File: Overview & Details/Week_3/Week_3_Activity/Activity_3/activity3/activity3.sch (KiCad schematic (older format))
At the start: 2 parts, among them J1 62684-502100ALF, U3 DISP_TFT_2.8IN_240x320_50PIN

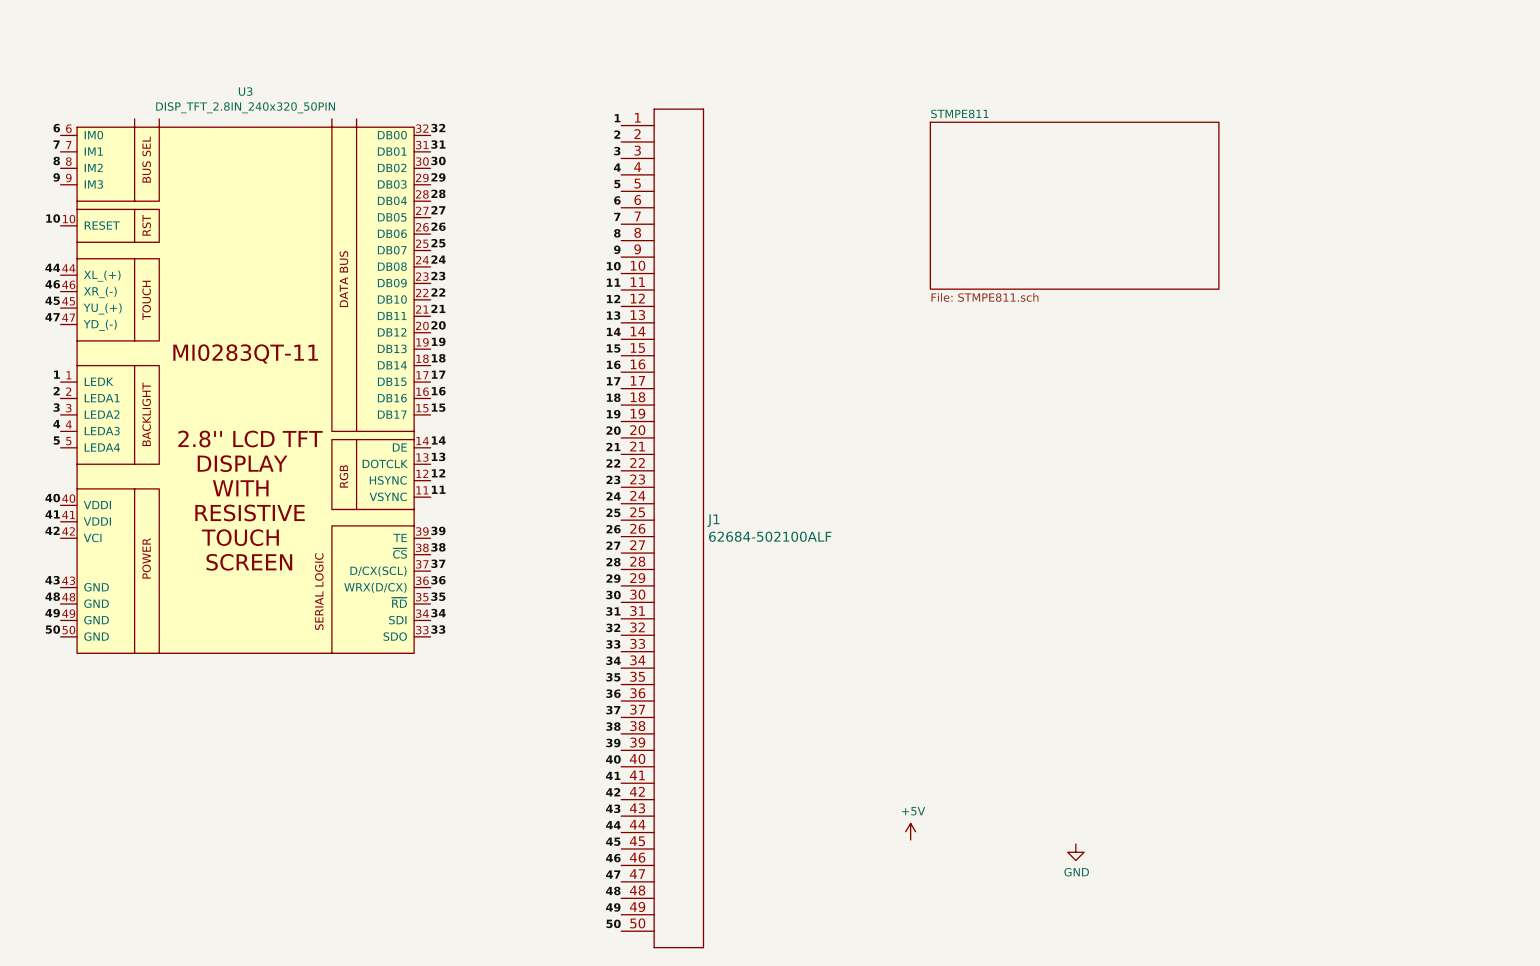
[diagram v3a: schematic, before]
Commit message: added STEMP811 controller and added pins
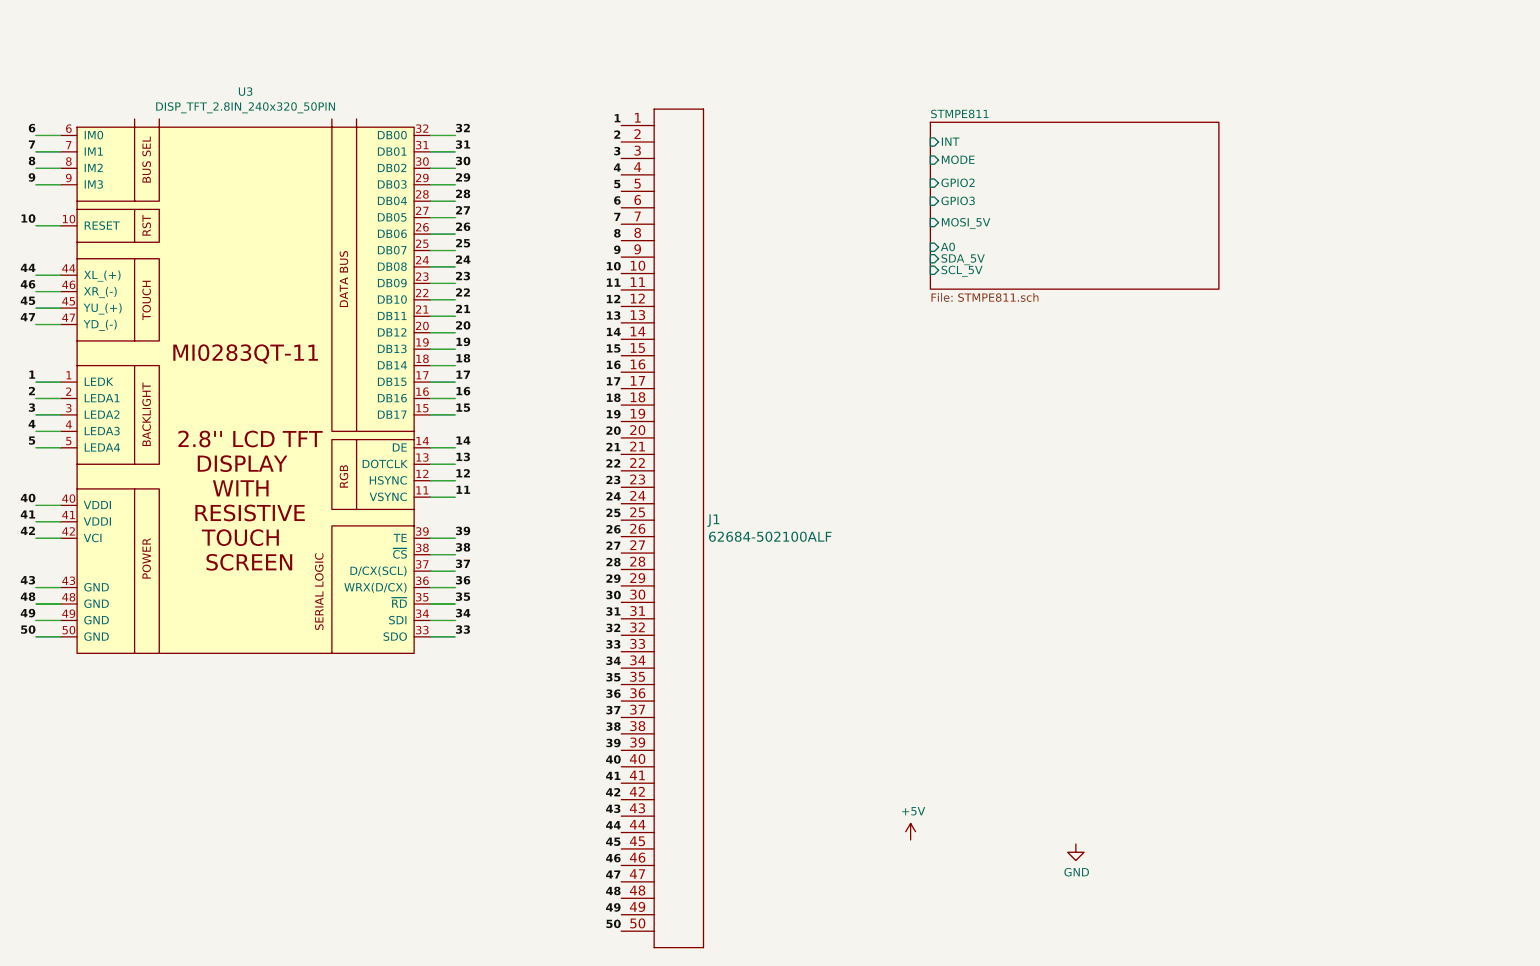
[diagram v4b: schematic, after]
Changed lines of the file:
@@
 F0 "STMPE811" 50
 F1 "STMPE811.sch" 50
+F2 "INT" I L 7330 1490 50
+F3 "MODE" I L 7330 1600 50
+F4 "GPIO2" I L 7330 1740 50
+F5 "GPIO3" I L 7330 1850 50
+F6 "MOSI_5V" I L 7330 1980 50
+F7 "A0" I L 7330 2130 50
+F8 "SCL_5V" I L 7330 2270 50
+F9 "SDA_5V" I L 7330 2200 50
 $EndSheet
 $Comp
@@
 	1    0    0    -1
 $EndComp
-Text Label 4290 1450 0    50   ~ 10
+Text Label 4440 1450 0    50   ~ 10
 32
-Text Label 4290 1550 0    50   ~ 10
+Text Label 4440 1550 0    50   ~ 10
 31
-Text Label 4290 1650 0    50   ~ 10
+Text Label 4440 1650 0    50   ~ 10
 30
-Text Label 4290 1750 0    50   ~ 10
+Text Label 4440 1750 0    50   ~ 10
 29
 Text Label 5450 4490 2    50   ~ 10
@@
 Text Label 5450 4190 2    50   ~ 10
 29
-Text Label 4290 1850 0    50   ~ 10
+Text Label 4440 1850 0    50   ~ 10
 28
-Text Label 4290 1950 0    50   ~ 10
+Text Label 4440 1950 0    50   ~ 10
 27
-Text Label 4290 2050 0    50   ~ 10
+Text Label 4440 2050 0    50   ~ 10
 26
-Text Label 4290 2150 0    50   ~ 10
+Text Label 4440 2150 0    50   ~ 10
 25
-Text Label 4290 2250 0    50   ~ 10
+Text Label 4440 2250 0    50   ~ 10
 24
-Text Label 4290 2350 0    50   ~ 10
+Text Label 4440 2350 0    50   ~ 10
 23
-Text Label 4290 2450 0    50   ~ 10
+Text Label 4440 2450 0    50   ~ 10
 22
-Text Label 4290 2550 0    50   ~ 10
+Text Label 4440 2550 0    50   ~ 10
 21
-Text Label 4290 2650 0    50   ~ 10
+Text Label 4440 2650 0    50   ~ 10
 20
-Text Label 4290 2750 0    50   ~ 10
+Text Label 4440 2750 0    50   ~ 10
 19
-Text Label 4290 2850 0    50   ~ 10
+Text Label 4440 2850 0    50   ~ 10
 18
-Text Label 4290 2950 0    50   ~ 10
+Text Label 4440 2950 0    50   ~ 10
 17
-Text Label 4290 3050 0    50   ~ 10
+Text Label 4440 3050 0    50   ~ 10
 16
-Text Label 4290 3150 0    50   ~ 10
+Text Label 4440 3150 0    50   ~ 10
 15
 Text Label 5450 4090 2    50   ~ 10
@@
 Text Label 5450 2790 2    50   ~ 10
 15
-Text Label 4290 3350 0    50   ~ 10
+Text Label 4440 3350 0    50   ~ 10
 14
-Text Label 4290 3450 0    50   ~ 10
+Text Label 4440 3450 0    50   ~ 10
 13
-Text Label 4290 3550 0    50   ~ 10
+Text Label 4440 3550 0    50   ~ 10
 12
-Text Label 4290 3650 0    50   ~ 10
+Text Label 4440 3650 0    50   ~ 10
 11
 Text Label 5450 2690 2    50   ~ 10
@@
 Text Label 5450 2390 2    50   ~ 10
 11
-Text Label 4290 3900 0    50   ~ 10
+Text Label 4440 3900 0    50   ~ 10
 39
-Text Label 4290 4000 0    50   ~ 10
+Text Label 4440 4000 0    50   ~ 10
 38
-Text Label 4290 4100 0    50   ~ 10
+Text Label 4440 4100 0    50   ~ 10
 37
-Text Label 4290 4200 0    50   ~ 10
+Text Label 4440 4200 0    50   ~ 10
 36
-Text Label 4290 4300 0    50   ~ 10
+Text Label 4440 4300 0    50   ~ 10
 35
-Text Label 4290 4400 0    50   ~ 10
+Text Label 4440 4400 0    50   ~ 10
 34
-Text Label 4290 4500 0    50   ~ 10
+Text Label 4440 4500 0    50   ~ 10
 33
 Text Label 5450 5190 2    50   ~ 10
@@
 Text Label 5450 4590 2    50   ~ 10
 33
-Text Label 2040 4200 2    50   ~ 10
+Text Label 1890 4200 2    50   ~ 10
 43
-Text Label 2040 3900 2    50   ~ 10
+Text Label 1890 3900 2    50   ~ 10
 42
-Text Label 2040 3800 2    50   ~ 10
+Text Label 1890 3800 2    50   ~ 10
 41
-Text Label 2040 3700 2    50   ~ 10
+Text Label 1890 3700 2    50   ~ 10
 40
 Text Label 5450 5490 2    50   ~ 10
@@
 Text Label 5450 5590 2    50   ~ 10
 43
-Text Label 2040 4300 2    50   ~ 10
+Text Label 1890 4300 2    50   ~ 10
 48
-Text Label 2040 4400 2    50   ~ 10
+Text Label 1890 4400 2    50   ~ 10
 49
-Text Label 2040 4500 2    50   ~ 10
+Text Label 1890 4500 2    50   ~ 10
 50
 $Comp
@@
 Text Label 5450 6290 2    50   ~ 10
 50
-Text Label 2040 2950 2    50   ~ 10
+Text Label 1890 2950 2    50   ~ 10
 1
-Text Label 2040 3050 2    50   ~ 10
+Text Label 1890 3050 2    50   ~ 10
 2
-Text Label 2040 3150 2    50   ~ 10
+Text Label 1890 3150 2    50   ~ 10
 3
-Text Label 2040 3250 2    50   ~ 10
+Text Label 1890 3250 2    50   ~ 10
 4
-Text Label 2040 3350 2    50   ~ 10
+Text Label 1890 3350 2    50   ~ 10
 5
 Text Label 5450 1390 2    50   ~ 10
@@
 Text Label 5450 1790 2    50   ~ 10
 5
-Text Label 2040 2600 2    50   ~ 10
+Text Label 1890 2600 2    50   ~ 10
 47
-Text Label 2040 2500 2    50   ~ 10
+Text Label 1890 2500 2    50   ~ 10
 45
-Text Label 2040 2400 2    50   ~ 10
+Text Label 1890 2400 2    50   ~ 10
 46
-Text Label 2040 2300 2    50   ~ 10
+Text Label 1890 2300 2    50   ~ 10
 44
 Text Label 5450 5990 2    50   ~ 10
@@
 Text Label 5450 5690 2    50   ~ 10
 44
-Text Label 2040 2000 2    50   ~ 10
+Text Label 1890 2000 2    50   ~ 10
 10
-Text Label 2040 1750 2    50   ~ 10
+Text Label 1890 1750 2    50   ~ 10
 9
-Text Label 2040 1650 2    50   ~ 10
+Text Label 1890 1650 2    50   ~ 10
 8
-Text Label 2040 1550 2    50   ~ 10
+Text Label 1890 1550 2    50   ~ 10
 7
-Text Label 2040 1450 2    50   ~ 10
+Text Label 1890 1450 2    50   ~ 10
 6
 Text Label 5450 2290 2    50   ~ 10
@@
 Text Label 5450 1890 2    50   ~ 10
 6
+Wire Wire Line
+	4290 4500 4440 4500
+Wire Wire Line
+	4290 4400 4440 4400
+Wire Wire Line
+	4290 4300 4440 4300
+Wire Wire Line
+	4290 4200 4440 4200
+Wire Wire Line
+	4290 4100 4440 4100
+Wire Wire Line
+	4290 4000 4440 4000
+Wire Wire Line
+	4290 3900 4440 3900
+Wire Wire Line
+	4290 3650 4440 3650
+Wire Wire Line
+	4290 3550 4440 3550
+Wire Wire Line
+	4290 3450 4440 3450
+Wire Wire Line
+	4290 3350 4440 3350
+Wire Wire Line
+	4290 3150 4440 3150
+Wire Wire Line
+	4290 3050 4440 3050
+Wire Wire Line
+	4290 2950 4440 2950
+Wire Wire Line
+	4290 2850 4440 2850
+Wire Wire Line
+	4290 2750 4440 2750
+Wire Wire Line
+	4290 2650 4440 2650
+Wire Wire Line
+	4290 2550 4440 2550
+Wire Wire Line
+	4290 2450 4440 2450
+Wire Wire Line
+	4290 2350 4440 2350
+Wire Wire Line
+	4290 2250 4440 2250
+Wire Wire Line
+	4290 2150 4440 2150
+Wire Wire Line
+	4290 2050 4440 2050
+Wire Wire Line
+	4290 1950 4440 1950
+Wire Wire Line
+	4290 1850 4440 1850
+Wire Wire Line
+	4290 1750 4440 1750
+Wire Wire Line
+	4290 1650 4440 1650
+Wire Wire Line
+	4290 1550 4440 1550
+Wire Wire Line
+	4290 1450 4440 1450
+Wire Wire Line
+	1890 1650 2040 1650
+Wire Wire Line
+	1890 1550 2040 1550
+Wire Wire Line
+	1890 1450 2040 1450
+Wire Wire Line
+	1890 2950 2040 2950
+Wire Wire Line
+	1890 2600 2040 2600
+Wire Wire Line
+	1890 2500 2040 2500
+Wire Wire Line
+	1890 2400 2040 2400
+Wire Wire Line
+	1890 2300 2040 2300
+Wire Wire Line
+	1890 2000 2040 2000
+Wire Wire Line
+	1890 1750 2040 1750
+Wire Wire Line
+	1890 3900 2040 3900
+Wire Wire Line
+	1890 3800 2040 3800
+Wire Wire Line
+	1890 3700 2040 3700
+Wire Wire Line
+	1890 3350 2040 3350
+Wire Wire Line
+	1890 3250 2040 3250
+Wire Wire Line
+	1890 3150 2040 3150
+Wire Wire Line
+	1890 3050 2040 3050
+Wire Wire Line
+	1890 4500 2040 4500
+Wire Wire Line
+	1890 4400 2040 4400
+Wire Wire Line
+	1890 4300 2040 4300
+Wire Wire Line
+	1890 4200 2040 4200
 $EndSCHEMATC

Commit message: added hierarchical pins to STMPE811
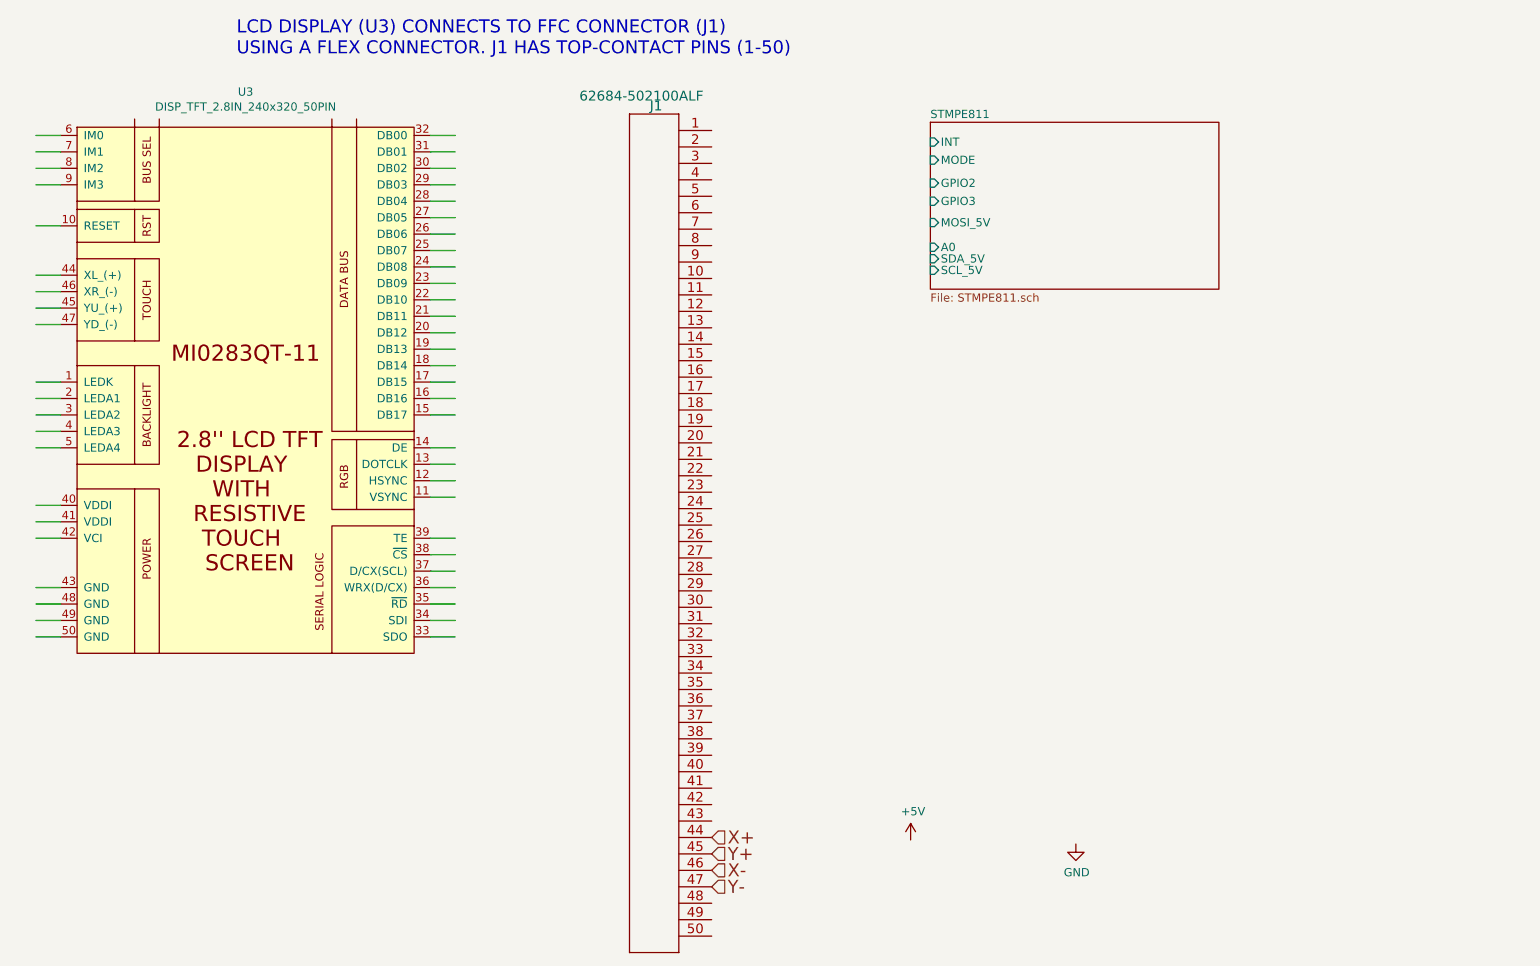
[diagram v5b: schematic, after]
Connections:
- net labels added: X+, X-, Y+, Y-
- net labels removed: 1, 10, 11, 12, 13, 14, 15, 16, 17, 18, 19, 2, 20, 21, 22, 23, 24, 25, 26, 27, 28, 29, 3, 30, 31, 32, 33, 34, 35, 36, 37, 38, 39, 4, 40, 41, 42, 43, 44, 45, 46, 47, 48, 49, 5, 50, 6, 7, 8, 9
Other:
- note added: "LCD DISPLAY (U3) CONNECTS TO FFC CONNECTOR (J1) \nUSING A FLEX CONNECTOR. J1 HAS TOP-CONTACT PINS (1-50)"
- moved on the sheet: J1
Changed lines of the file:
@@
 L 2020-04-05_01-22-35:62684-502100ALF J1
 U 1 1 5F061D23
-P 5450 1390
-F 0 "J1" H 5978 -1007 60  0000 L CNN
-F 1 "62684-502100ALF" H 5978 -1113 60  0000 L CNN
-F 2 "CONN50_62684-502100ALF" H 5850 -1070 60  0001 C CNN
-F 3 "" H 5450 1390 60  0000 C CNN
-	1    5450 1390
-	1    0    0    -1
+P 6000 1420
+F 0 "J1" H 6300 1570 60  0000 L CNN
+F 1 "62684-502100ALF" H 6050 1630 60  0000 L CNN
+F 2 "CONN50_62684-502100ALF" H 6400 -1040 60  0001 C CNN
+F 3 "" H 6000 1420 60  0000 C CNN
+	1    6000 1420
+	-1   0    0    -1
 $EndComp
-Text Label 4440 1450 0    50   ~ 10
-32
-Text Label 4440 1550 0    50   ~ 10
-31
-Text Label 4440 1650 0    50   ~ 10
-30
-Text Label 4440 1750 0    50   ~ 10
-29
-Text Label 5450 4490 2    50   ~ 10
-32
-Text Label 5450 4390 2    50   ~ 10
-31
-Text Label 5450 4290 2    50   ~ 10
-30
-Text Label 5450 4190 2    50   ~ 10
-29
-Text Label 4440 1850 0    50   ~ 10
-28
-Text Label 4440 1950 0    50   ~ 10
-27
-Text Label 4440 2050 0    50   ~ 10
-26
-Text Label 4440 2150 0    50   ~ 10
-25
-Text Label 4440 2250 0    50   ~ 10
-24
-Text Label 4440 2350 0    50   ~ 10
-23
-Text Label 4440 2450 0    50   ~ 10
-22
-Text Label 4440 2550 0    50   ~ 10
-21
-Text Label 4440 2650 0    50   ~ 10
-20
-Text Label 4440 2750 0    50   ~ 10
-19
-Text Label 4440 2850 0    50   ~ 10
-18
-Text Label 4440 2950 0    50   ~ 10
-17
-Text Label 4440 3050 0    50   ~ 10
-16
-Text Label 4440 3150 0    50   ~ 10
-15
-Text Label 5450 4090 2    50   ~ 10
-28
-Text Label 5450 3990 2    50   ~ 10
-27
-Text Label 5450 3890 2    50   ~ 10
-26
-Text Label 5450 3790 2    50   ~ 10
-25
-Text Label 5450 3690 2    50   ~ 10
-24
-Text Label 5450 3590 2    50   ~ 10
-23
-Text Label 5450 3490 2    50   ~ 10
-22
-Text Label 5450 3390 2    50   ~ 10
-21
-Text Label 5450 3290 2    50   ~ 10
-20
-Text Label 5450 3190 2    50   ~ 10
-19
-Text Label 5450 3090 2    50   ~ 10
-18
-Text Label 5450 2990 2    50   ~ 10
-17
-Text Label 5450 2890 2    50   ~ 10
-16
-Text Label 5450 2790 2    50   ~ 10
-15
-Text Label 4440 3350 0    50   ~ 10
-14
-Text Label 4440 3450 0    50   ~ 10
-13
-Text Label 4440 3550 0    50   ~ 10
-12
-Text Label 4440 3650 0    50   ~ 10
-11
-Text Label 5450 2690 2    50   ~ 10
-14
-Text Label 5450 2590 2    50   ~ 10
-13
-Text Label 5450 2490 2    50   ~ 10
-12
-Text Label 5450 2390 2    50   ~ 10
-11
-Text Label 4440 3900 0    50   ~ 10
-39
-Text Label 4440 4000 0    50   ~ 10
-38
-Text Label 4440 4100 0    50   ~ 10
-37
-Text Label 4440 4200 0    50   ~ 10
-36
-Text Label 4440 4300 0    50   ~ 10
-35
-Text Label 4440 4400 0    50   ~ 10
-34
-Text Label 4440 4500 0    50   ~ 10
-33
-Text Label 5450 5190 2    50   ~ 10
-39
-Text Label 5450 5090 2    50   ~ 10
-38
-Text Label 5450 4990 2    50   ~ 10
-37
-Text Label 5450 4890 2    50   ~ 10
-36
-Text Label 5450 4790 2    50   ~ 10
-35
-Text Label 5450 4690 2    50   ~ 10
-34
-Text Label 5450 4590 2    50   ~ 10
-33
-Text Label 1890 4200 2    50   ~ 10
-43
-Text Label 1890 3900 2    50   ~ 10
-42
-Text Label 1890 3800 2    50   ~ 10
-41
-Text Label 1890 3700 2    50   ~ 10
-40
-Text Label 5450 5490 2    50   ~ 10
-42
-Text Label 5450 5390 2    50   ~ 10
-41
-Text Label 5450 5290 2    50   ~ 10
-40
-Text Label 5450 5590 2    50   ~ 10
-43
-Text Label 1890 4300 2    50   ~ 10
-48
-Text Label 1890 4400 2    50   ~ 10
-49
-Text Label 1890 4500 2    50   ~ 10
-50
 $Comp
 L Display_Board_Lib:DISP_TFT_2.8IN_240x320_50PIN U3
@@
 	1    0    0    -1
 $EndComp
-Text Label 5450 6090 2    50   ~ 10
-48
-Text Label 5450 6190 2    50   ~ 10
-49
-Text Label 5450 6290 2    50   ~ 10
-50
-Text Label 1890 2950 2    50   ~ 10
-1
-Text Label 1890 3050 2    50   ~ 10
-2
-Text Label 1890 3150 2    50   ~ 10
-3
-Text Label 1890 3250 2    50   ~ 10
-4
-Text Label 1890 3350 2    50   ~ 10
-5
-Text Label 5450 1390 2    50   ~ 10
-1
-Text Label 5450 1490 2    50   ~ 10
-2
-Text Label 5450 1590 2    50   ~ 10
-3
-Text Label 5450 1690 2    50   ~ 10
-4
-Text Label 5450 1790 2    50   ~ 10
-5
-Text Label 1890 2600 2    50   ~ 10
-47
-Text Label 1890 2500 2    50   ~ 10
-45
-Text Label 1890 2400 2    50   ~ 10
-46
-Text Label 1890 2300 2    50   ~ 10
-44
-Text Label 5450 5990 2    50   ~ 10
-47
-Text Label 5450 5790 2    50   ~ 10
-45
-Text Label 5450 5890 2    50   ~ 10
-46
-Text Label 5450 5690 2    50   ~ 10
-44
-Text Label 1890 2000 2    50   ~ 10
-10
-Text Label 1890 1750 2    50   ~ 10
-9
-Text Label 1890 1650 2    50   ~ 10
-8
-Text Label 1890 1550 2    50   ~ 10
-7
-Text Label 1890 1450 2    50   ~ 10
-6
-Text Label 5450 2290 2    50   ~ 10
-10
-Text Label 5450 2190 2    50   ~ 10
-9
-Text Label 5450 2090 2    50   ~ 10
-8
-Text Label 5450 1990 2    50   ~ 10
-7
-Text Label 5450 1890 2    50   ~ 10
-6
 Wire Wire Line
 	4290 4500 4440 4500
@@
 Wire Wire Line
 	1890 4200 2040 4200
+Text Notes 3110 970  0    79   ~ 0
+LCD DISPLAY (U3) CONNECTS TO FFC CONNECTOR (J1) \nUSING A FLEX CONNECTOR. J1 HAS TOP-CONTACT PINS (1-50)
+Text HLabel 6000 5720 2    79   Input ~ 0
+X+
+Text HLabel 6000 5820 2    79   Input ~ 0
+Y+
+Text HLabel 6000 5920 2    79   Input ~ 0
+X-
+Text HLabel 6000 6020 2    79   Input ~ 0
+Y-
 $EndSCHEMATC
